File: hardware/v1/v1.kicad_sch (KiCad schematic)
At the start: 70 parts, among them J1 AUDIO IN, J2 MIDI OUT, J3 MIDI IN, J4 MIDI THRU, J5 OUTPUT R, J6 OUTPUT L - MONO, J7 EXP 2, J8 EXP 1, J9 Conn_01x02_Female, SW1 RotaryEncoder_Switch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

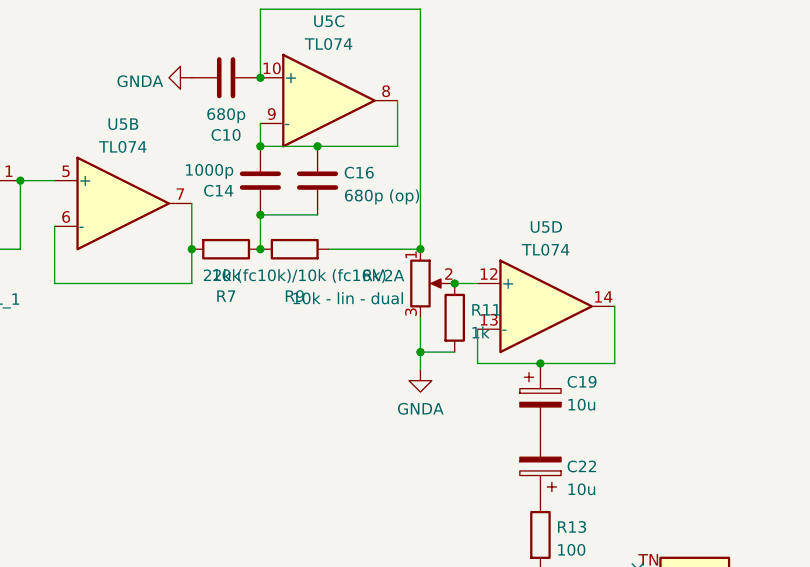
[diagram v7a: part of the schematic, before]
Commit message: Assignation of easy components
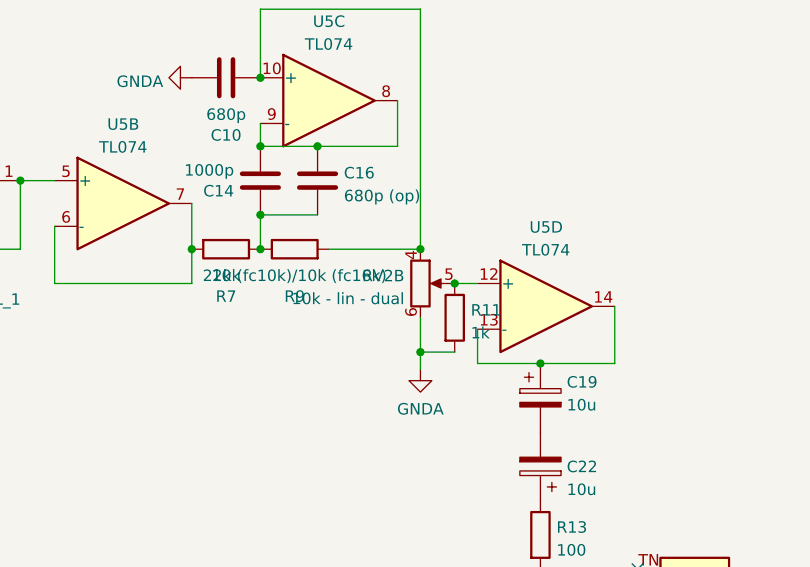
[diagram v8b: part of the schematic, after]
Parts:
- C1, C11, C12, C24, C3: footprint (none) -> Capacitor_THT:C_Axial_L3.8mm_D2.6mm_P7.50mm_Horizontal
- C17, C18, C19, C20, C21, C22: footprint (none) -> Capacitor_THT:CP_Radial_D5.0mm_P2.50mm
- C2: footprint (none) -> Capacitor_THT:CP_Radial_D10.0mm_P3.80mm
- C23: footprint (none) -> Capacitor_THT:CP_Radial_D7.5mm_P2.50mm
- D1: footprint (none) -> Diode_THT:D_DO-34_SOD68_P7.62mm_Horizontal
- J9: footprint (none) -> Connector_JST:JST_XH_B2B-XH-AM_1x02_P2.50mm_Vertical
- RV3, RV4, RV5: footprint (none) -> Potentiometer_THT:Potentiometer_Alps_RK09K_Single_Vertical
- SW1: footprint (none) -> Rotary_Encoder:RotaryEncoder_Alps_EC11E-Switch_Vertical_H20mm
- U2: footprint RPi_Pico:RPi_Pico_SMD_TH -> Pi Pico:RPi_Pico_SMD_TH
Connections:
- net GNDA: now also RV2.6; no longer RV2.3
- net at R11.1, U5.12 (+): now also RV2.5; no longer RV2.2
- net at C10.2, R9.2, U5.10 (+): now also RV2.4; no longer RV2.1
